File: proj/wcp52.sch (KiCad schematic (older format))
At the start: 9 parts, among them J2 IN1, J3 IN2, J4 OUT, J5 CONN-PJ-037A, J7 AUX

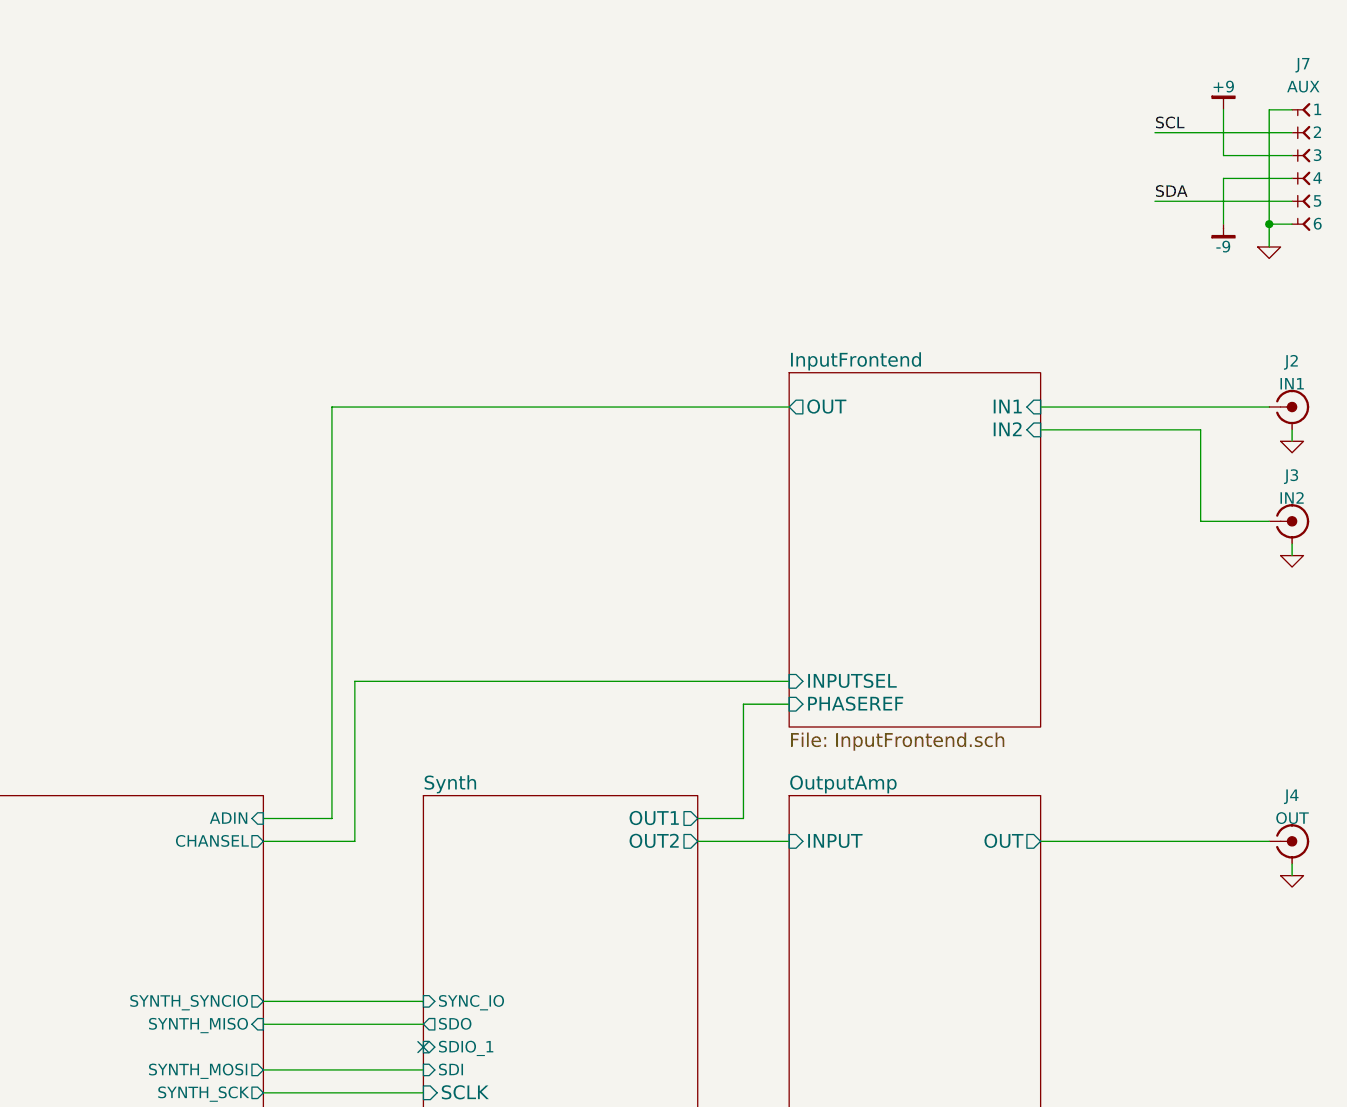
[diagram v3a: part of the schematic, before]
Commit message: Add I2C to header
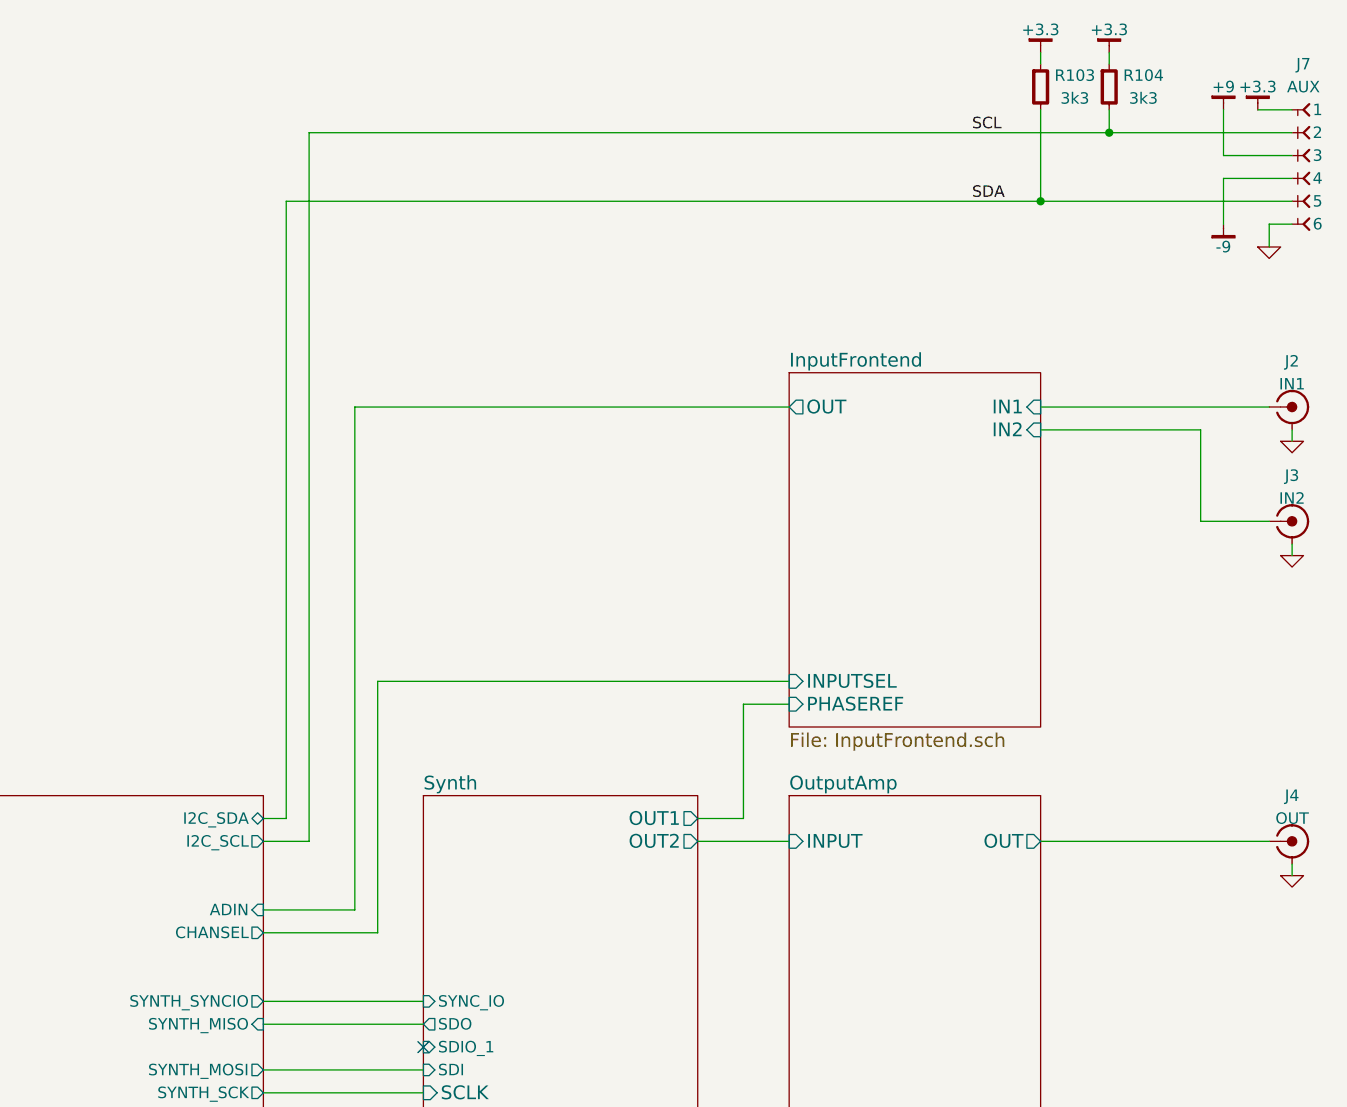
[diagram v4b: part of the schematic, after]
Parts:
- added R103, R104: 3k3, IPC7351-Nominal:RESC1005X40, symbol R-0402
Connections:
- net +3.3: now also J7.1, R103.1, R104.1
- net GND: no longer J7.1
- net SCL: now also R104.2
- net SDA: now also R103.2
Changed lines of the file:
@@
 $EndDescr
-$Sheet
-S 5400 4000 2900 1800
-U 54F1FAC6
-F0 "MPU" 60
-F1 "MPU.sch" 60
-F2 "USBD_N" B L 5400 5500 50
-F3 "USBD_P" B L 5400 5600 50
-F4 "SER_TO_MPU" I L 5400 4500 50
-F5 "SER_FROM_MPU" O L 5400 4600 50
-F6 "SYNTH_#CS" O R 8300 5400 50
-F7 "SYNTH_IOUPDATE" O R 8300 5700 50
-F8 "SYNTH_PWRDN" O R 8300 5500 50
-F9 "SYNTH_MRST" O R 8300 5600 50
-F10 "SYNTH_SYNCIO" O R 8300 4900 50
-F11 "CHANSEL" O R 8300 4200 50
-F12 "SYNTH_SCK" O R 8300 5300 50
-F13 "SYNTH_MISO" I R 8300 5000 50
-F14 "SYNTH_MOSI" O R 8300 5200 50
-F15 "ADIN" I R 8300 4100 50
-$EndSheet
 $Sheet
 S 1900 4000 1300 1800
@@
 NoConn ~ 9000 5100
 Wire Wire Line
-	8300 4200 8700 4200
-Wire Wire Line
-	8700 4200 8700 3500
-Wire Wire Line
-	8700 3500 10600 3500
-Wire Wire Line
-	8300 4100 8600 4100
-Wire Wire Line
-	8600 4100 8600 2300
-Wire Wire Line
-	8600 2300 10600 2300
+	8300 4600 8800 4600
+Wire Wire Line
+	8800 4600 8800 3500
+Wire Wire Line
+	8800 3500 10600 3500
+Wire Wire Line
+	8300 4500 8700 4500
+Wire Wire Line
+	8700 4500 8700 2300
+Wire Wire Line
+	8700 2300 10600 2300
 $Comp
 L CONN-100MIL-F-1x6 J7
@@
 $EndComp
 Wire Wire Line
-	12800 1000 12700 1000
-Wire Wire Line
-	12700 1000 12700 1600
+	12650 1000 12800 1000
 Wire Wire Line
 	12800 1500 12700 1500
-Connection ~ 12700 1500
 $Comp
 L GND #PWR016
@@
 $EndComp
 Wire Wire Line
-	12800 1100 12200 1100
-Text Label 12200 1100 0    50   ~ 0
+	8500 1100 12800 1100
+Text Label 11400 1100 0    50   ~ 0
 SCL
-Text Label 12200 1400 0    50   ~ 0
+Text Label 11400 1400 0    50   ~ 0
 SDA
 Wire Wire Line
-	12200 1400 12800 1400
+	8400 1400 12800 1400
 Wire Wire Line
 	12800 1200 12500 1200
@@
 Wire Wire Line
 	12500 1300 12800 1300
+Wire Wire Line
+	12700 1500 12700 1600
+$Comp
+L +3.3 #PWR019
+U 1 1 54FBE2D0
+P 12650 1000
+F 0 "#PWR019" H 12650 1050 30  0001 C CNN
+F 1 "+3.3" H 12650 1100 50  0000 C CNN
+F 2 "" H 12650 1000 60  0000 C CNN
+F 3 "" H 12650 1000 60  0000 C CNN
+	1    12650 1000
+	1    0    0    -1
+$EndComp
+$Comp
+L R-0402 R103
+U 1 1 54FC0A2D
+P 11700 900
+F 0 "R103" H 11850 950 50  0000 C CNN
+F 1 "3k3" H 11850 850 50  0000 C CNN
+F 2 "IPC7351-Nominal:RESC1005X40" H 11700 900 50  0001 C CNN
+F 3 "" H 11700 950 60  0000 C CNN
+F 4 "Value" H 11700 900 60  0001 C CNN "Manuf"
+F 5 "RES SMD 3.3k 5% [0402]" H 12450 1450 60  0001 C CNN "BOM"
+	1    11700 900
+	1    0    0    -1
+$EndComp
+$Comp
+L R-0402 R104
+U 1 1 54FC0C4B
+P 12000 900
+F 0 "R104" H 12150 950 50  0000 C CNN
+F 1 "3k3" H 12150 850 50  0000 C CNN
+F 2 "IPC7351-Nominal:RESC1005X40" H 12000 900 50  0001 C CNN
+F 3 "" H 12000 950 60  0000 C CNN
+F 4 "Value" H 12000 900 60  0001 C CNN "Manuf"
+F 5 "RES SMD 3.3k 5% [0402]" H 12750 1450 60  0001 C CNN "BOM"
+	1    12000 900
+	1    0    0    -1
+$EndComp
+$Comp
+L +3.3 #PWR020
+U 1 1 54FC0D1C
+P 11700 750
+F 0 "#PWR020" H 11700 800 30  0001 C CNN
+F 1 "+3.3" H 11700 850 50  0000 C CNN
+F 2 "" H 11700 750 60  0000 C CNN
+F 3 "" H 11700 750 60  0000 C CNN
+	1    11700 750
+	1    0    0    -1
+$EndComp
+Wire Wire Line
+	11700 750  11700 800
+$Comp
+L +3.3 #PWR021
+U 1 1 54FC0EC7
+P 12000 750
+F 0 "#PWR021" H 12000 800 30  0001 C CNN
+F 1 "+3.3" H 12000 850 50  0000 C CNN
+F 2 "" H 12000 750 60  0000 C CNN
+F 3 "" H 12000 750 60  0000 C CNN
+	1    12000 750
+	1    0    0    -1
+$EndComp
+Wire Wire Line
+	12000 750  12000 800
+Wire Wire Line
+	12000 1000 12000 1100
+Connection ~ 12000 1100
+Wire Wire Line
+	11700 1000 11700 1400
+Connection ~ 11700 1400
+$Sheet
+S 5400 4000 2900 1800
+U 54F1FAC6
+F0 "MPU" 60
+F1 "MPU.sch" 60
+F2 "USBD_N" B L 5400 5500 50
+F3 "USBD_P" B L 5400 5600 50
+F4 "SER_TO_MPU" I L 5400 4500 50
+F5 "SER_FROM_MPU" O L 5400 4600 50
+F6 "SYNTH_#CS" O R 8300 5400 50
+F7 "SYNTH_IOUPDATE" O R 8300 5700 50
+F8 "SYNTH_PWRDN" O R 8300 5500 50
+F9 "SYNTH_MRST" O R 8300 5600 50
+F10 "SYNTH_SYNCIO" O R 8300 4900 50
+F11 "CHANSEL" O R 8300 4600 50
+F12 "SYNTH_SCK" O R 8300 5300 50
+F13 "SYNTH_MISO" I R 8300 5000 50
+F14 "SYNTH_MOSI" O R 8300 5200 50
+F15 "ADIN" I R 8300 4500 50
+F16 "I2C_SDA" B R 8300 4100 50
+F17 "I2C_SCL" O R 8300 4200 50
+$EndSheet
+Wire Wire Line
+	8300 4100 8400 4100
+Wire Wire Line
+	8400 4100 8400 1400
+Wire Wire Line
+	8300 4200 8500 4200
+Wire Wire Line
+	8500 4200 8500 1100
 $EndSCHEMATC

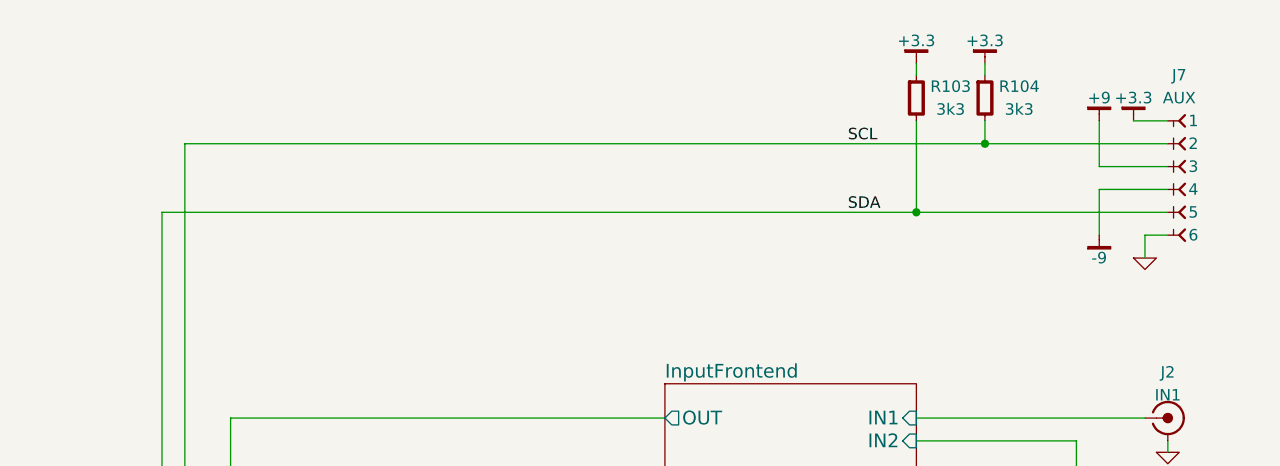
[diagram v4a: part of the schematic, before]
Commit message: Add overload protection to aux power output
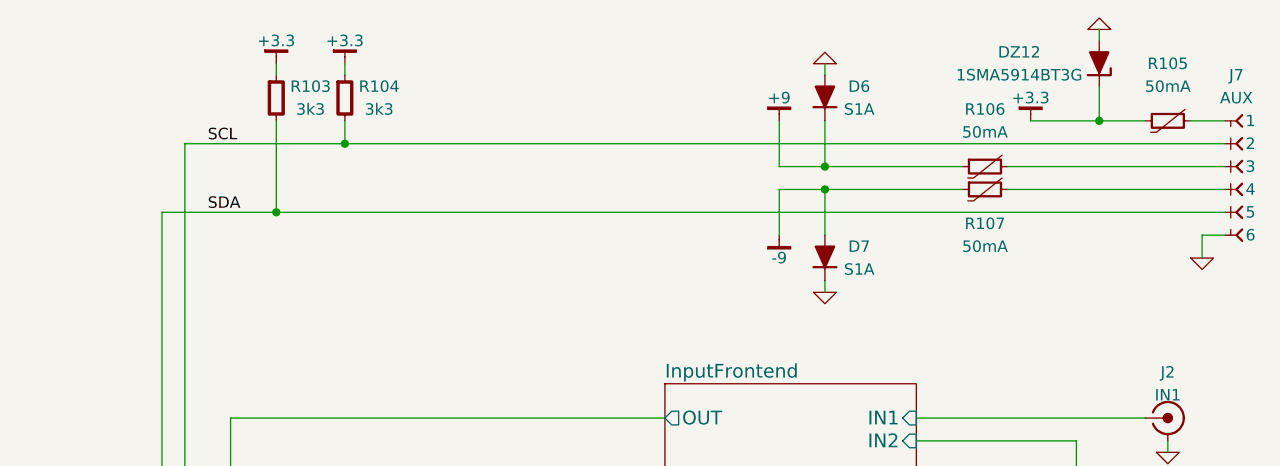
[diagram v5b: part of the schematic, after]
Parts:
- added D6, D7: S1A, IPC7351-Nominal:DIOM5326X292, symbol S1A
- added DZ12: 1SMA5914BT3G, IPC7351-Nominal:DIOM5226X203, symbol 1SMA59xxBT3G
- added R105, R106, R107: 50mA, IPC7351-Nominal:RESC3216X60, symbol THERM
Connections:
- net +3.3: now also DZ12.1, R105.1; no longer J7.1
- net +9: now also D6.1, R106.1; no longer J7.3
- net -9: now also D7.2, R107.1; no longer J7.4
- net GND: now also D6.2, D7.1, DZ12.2
- new net: J7.1, R105.2
- new net: J7.3, R106.2
- new net: J7.4, R107.2
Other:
- moved on the sheet: J7, R103, R104

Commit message: Connect attenuator control
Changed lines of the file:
@@
 $EndComp
 $Sheet
-S 5400 4000 2900 1800
+S 5400 4000 2900 2000
 U 54F1FAC6
 F0 "MPU" 60
@@
 F16 "I2C_SDA" B R 8300 4100 50
 F17 "I2C_SCL" O R 8300 4200 50
+F18 "ATTEN" O R 8300 5900 50
 $EndSheet
 $Comp
@@
 Wire Wire Line
 	12500 600  12500 650
+Wire Wire Line
+	8300 5900 10450 5900
+Wire Wire Line
+	10450 5900 10450 5700
+Wire Wire Line
+	10450 5700 10600 5700
 $EndSCHEMATC

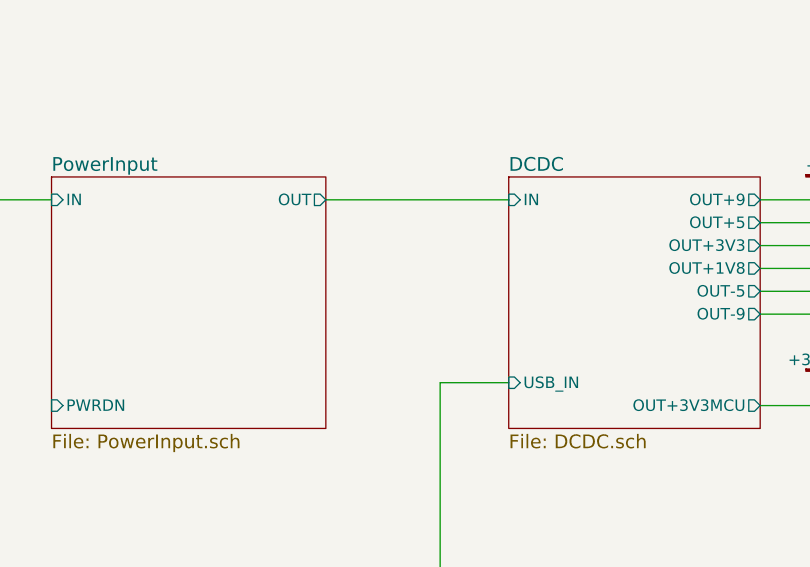
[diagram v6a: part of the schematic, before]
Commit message: Add power LED
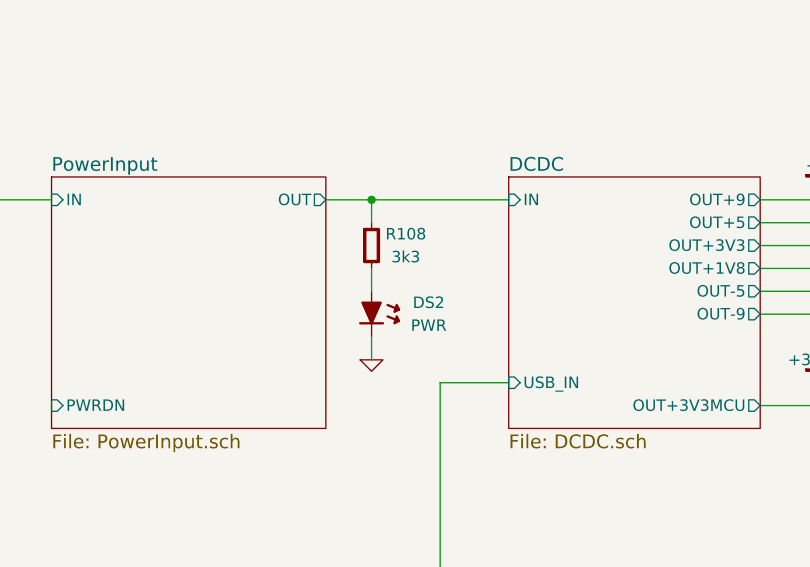
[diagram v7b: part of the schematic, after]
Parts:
- added DS2: PWR, smd-semi:LED-0603, symbol LED-0603
- added R108: 3k3, IPC7351-Nominal:RESC1005X40, symbol R-0402
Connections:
- net DCDC/IN: now also R108.1
- net GND: now also DS2.1
- new net: DS2.2, R108.2
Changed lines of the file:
@@
 Wire Wire Line
 	10450 5700 10600 5700
+$Comp
+L R-0402 R108
+U 1 1 54FCBDC0
+P 3300 1900
+F 0 "R108" H 3450 1950 50  0000 C CNN
+F 1 "3k3" H 3450 1850 50  0000 C CNN
+F 2 "IPC7351-Nominal:RESC1005X40" H 3300 1900 50  0001 C CNN
+F 3 "" H 3300 1950 60  0000 C CNN
+F 4 "Value" H 3300 1900 60  0001 C CNN "Manuf"
+F 5 "RES SMD 3.3k 5% [0402]" H 4050 2450 60  0001 C CNN "BOM"
+	1    3300 1900
+	1    0    0    -1
+$EndComp
+Wire Wire Line
+	3300 1800 3300 1700
+Connection ~ 3300 1700
+$Comp
+L LED-0603 DS2
+U 1 1 54FCBFE5
+P 3300 2200
+F 0 "DS2" H 3550 2250 50  0000 C CNN
+F 1 "PWR" H 3550 2150 50  0000 C CNN
+F 2 "smd-semi:LED-0603" H 3300 2200 50  0001 C CNN
+F 3 "" H 3300 2200 60  0000 C CNN
+F 4 "Value" H 3300 2200 60  0001 C CNN "Manuf"
+F 5 "SEMI GENERIC LED RED [0603]" H 4150 2750 60  0001 C CNN "BOM"
+	1    3300 2200
+	1    0    0    -1
+$EndComp
+Wire Wire Line
+	3300 2100 3300 2000
+$Comp
+L GND #PWR025
+U 1 1 54FCC228
+P 3300 2400
+F 0 "#PWR025" H 3300 2400 30  0001 C CNN
+F 1 "GND" H 3300 2330 30  0001 C CNN
+F 2 "" H 3300 2400 60  0000 C CNN
+F 3 "" H 3300 2400 60  0000 C CNN
+	1    3300 2400
+	1    0    0    -1
+$EndComp
+Wire Wire Line
+	3300 2400 3300 2300
 $EndSCHEMATC
